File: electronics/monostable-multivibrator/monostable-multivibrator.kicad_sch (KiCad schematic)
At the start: 1 part, among them U1 NE555P

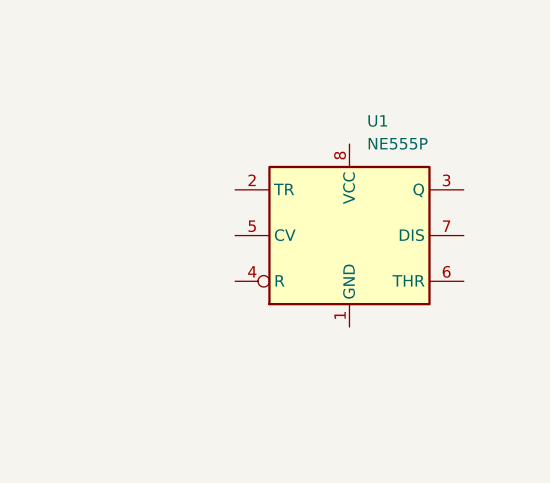
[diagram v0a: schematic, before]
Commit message: adding basic schematic
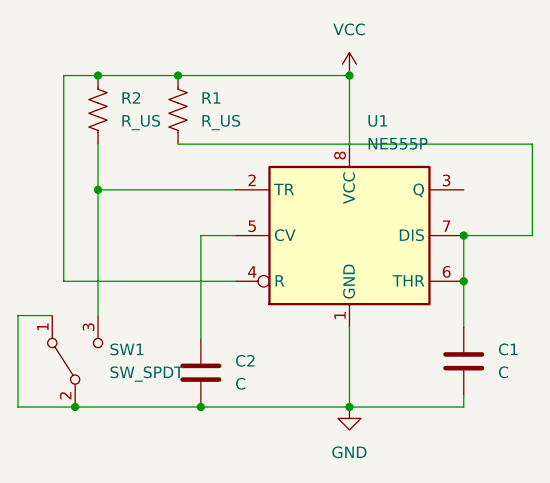
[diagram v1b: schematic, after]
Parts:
- added C1, C2: C, symbol Device:C
- added R1, R2: R_US, symbol Device:R_US
- added SW1: SW_SPDT, symbol Switch:SW_SPDT
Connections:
- net GND: now reaches U1.1 (GND)
- net GND: now also C1.2, C2.2, SW1.1 (A), SW1.2 (B)
- net at U1.2 (TR): now also R2.2, SW1.3 (C)
- net VCC: now reaches U1.4 (R)
- net VCC: now also U1.8 (VCC), R1.1, R2.1
- net at U1.5 (CV): now also C2.1
- net at U1.6 (THR): now also U1.7 (DIS), C1.1, R1.2

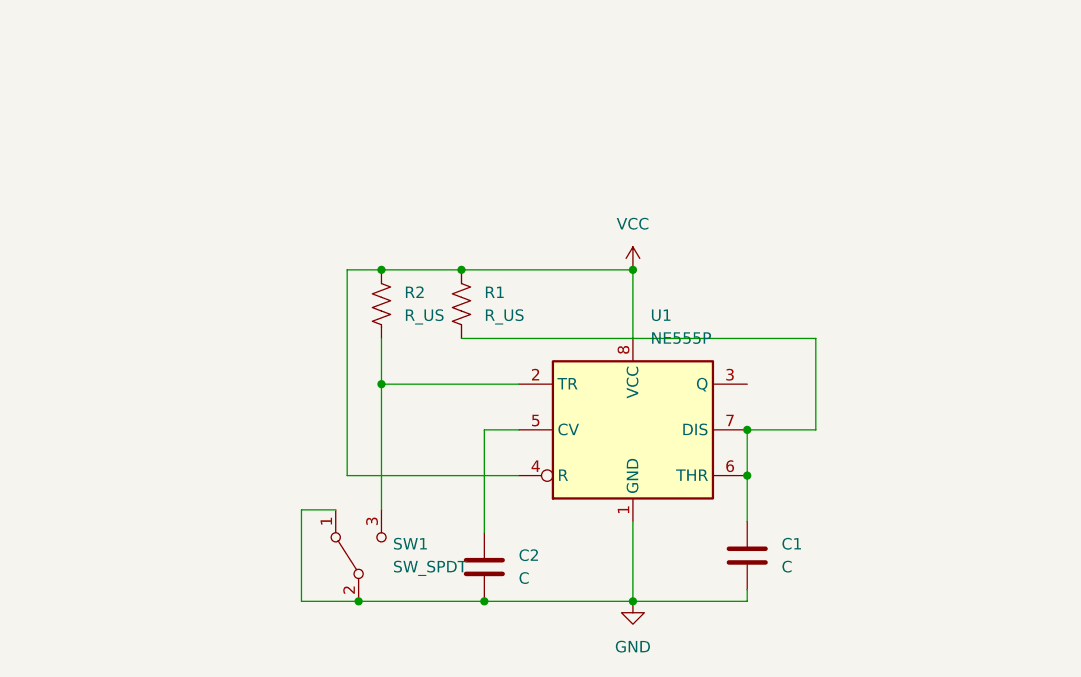
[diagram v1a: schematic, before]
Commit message: adding more components
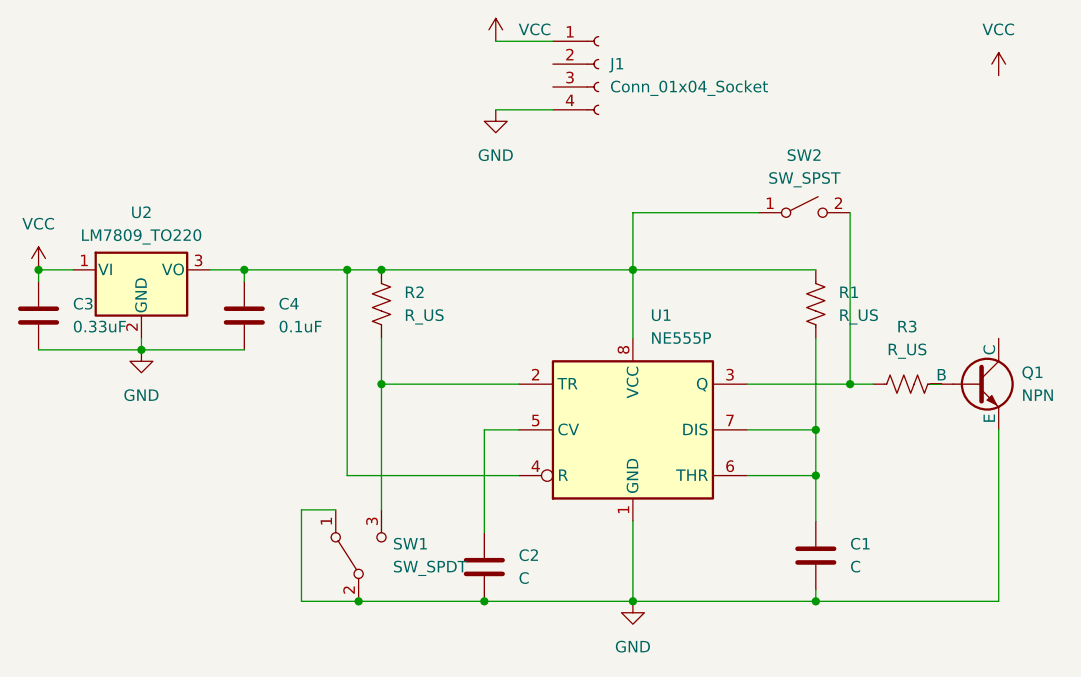
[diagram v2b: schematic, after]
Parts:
- added C3: 0.33uF, symbol Device:C
- added C4: 0.1uF, symbol Device:C
- added J1: Conn_01x04_Socket, symbol Connector:Conn_01x04_Socket
- added Q1: NPN, symbol Simulation_SPICE:NPN
- added R3: R_US, symbol Device:R_US
- added SW2: SW_SPST, symbol Switch:SW_SPST
- added U2: LM7809_TO220, Package_TO_SOT_THT:TO-220-3_Vertical, symbol Regulator_Linear:LM7809_TO220
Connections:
- net GND: now also C3.2, C4.2, J1.4 (Pin_4), Q1.3 (E), U2.2 (GND)
- net VCC: now also C3.1, J1.1 (Pin_1), U2.1 (VI); no longer R1.1, R2.1, U1.4 (R), U1.8 (VCC)
- net at U1.3 (Q): now also R3.1, SW2.2 (B)
- new net: Q1.2 (B), R3.2
- new net: C4.1, R1.1, R2.1, SW2.1 (A), U1.4 (R), U1.8 (VCC), U2.3 (VO)
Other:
- moved on the sheet: C1, R1

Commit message: more updates
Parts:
- removed J1: Conn_01x04_Socket, symbol Connector:Conn_01x04_Socket
- removed R2: R_US, symbol Device:R_US
- removed SW2: SW_SPST, symbol Switch:SW_SPST
- added J1, J2, J3, J4, J5, J6, J7, J8: Conn_01x01_Socket, symbol Connector:Conn_01x01_Socket
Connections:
- net GND: now also J2.1 (Pin_1)
- net VCC: now also J1.1 (Pin_1), J7.1 (Pin_1)
- net at R3.1, U1.3 (Q): now also J6.1 (Pin_1)
- net at Q1.1 (C): now also J8.1 (Pin_1)
- net at C4.1, R1.1, U1.4 (R)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: now also J3.1 (Pin_1), J5.1 (Pin_1)
- net at SW1.3 (C), U1.2 (TR): now also R1.2
- net at C1.1, U1.6 (THR), U1.7 (DIS): now also J4.1 (Pin_1); no longer R1.2
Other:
- moved on the sheet: R1

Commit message: mostly finished
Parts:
- removed J5, J6, J7, J8: Conn_01x01_Socket, symbol Connector:Conn_01x01_Socket
- removed U2: LM7809_TO220, Package_TO_SOT_THT:TO-220-3_Vertical, symbol Regulator_Linear:LM7809_TO220
- added D1, D2: 1N4001, Diode_THT:D_DO-41_SOD81_P10.16mm_Horizontal, symbol Diode:1N4001
- added JP1: Jumper_2_Open, symbol Jumper:Jumper_2_Open
- added R2: POT, symbol Device:R_US
- added SW2: SW_BYPASS, symbol Switch:SW_SPST
- added U2: LM7805_TO220, Package_TO_SOT_THT:TO-220-3_Vertical, symbol Regulator_Linear:LM7805_TO220
- C2: value C -> 10nF
- J1: value Conn_01x01_Socket -> VCC_IN
- J2: value Conn_01x01_Socket -> EXT_GND
- J3: value Conn_01x01_Socket -> LOAD_VIN
- J4: value Conn_01x01_Socket -> LOAD_COM
- Q1: value NPN -> 2N2222
- R1: value R_US -> 100K
- R3: value R_US -> 120
- SW1: value SW_SPDT -> SW_TRIG
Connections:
- net GND: now also C2.1, SW1.3 (C), D1.2 (A), U2.2 (GND); no longer C2.2, SW1.1 (A), SW1.2 (B)
- net VCC: now also J3.1 (Pin_1), JP1.1 (A), U2.1 (VI)
- net at R3.1: now also D2.1 (K), SW2.1 (A); no longer U1.3 (Q)
- net at C1.1, U1.6 (THR), U1.7 (DIS): now also R2.2; no longer J4.1 (Pin_1)
- net at Q1.1 (C): now also J4.1 (Pin_1), D1.1 (K)
- net at U1.5 (CV): now also C2.2; no longer C2.1
- net 555_VIN: now reaches C4.1, R1.1, U1.4 (R), U1.8 (VCC)
- net 555_VIN: now also JP1.2 (B), R2.1, SW2.2 (B), U2.3 (VO); no longer J3.1 (Pin_1)
- new net: SW1.2 (B), U1.2 (TR)
- new net: R1.2, SW1.1 (A)
- new net 555_OUT: D2.2 (A), U1.3 (Q)
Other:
- note added: "JUMPER IF VCC < 16V REG NOT NEEDED"
- note added: "T = 1.1 * R2 * C1"
- moved on the sheet: C1, C2, C3, C4, J1, J2, Q1, R1, R3, SW1, U1

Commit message: footprints
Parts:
- C1: footprint (none) -> Capacitor_THT:CP_Radial_D8.0mm_P3.80mm
- C2, C3, C4: footprint (none) -> Capacitor_THT:C_Disc_D3.0mm_W1.6mm_P2.50mm
- J1, J3, J4: footprint (none) -> Connector_PinHeader_1.00mm:PinHeader_1x01_P1.00mm_Horizontal
- J2: value EXT_GND -> GND_IN; footprint (none) -> Connector_PinHeader_1.00mm:PinHeader_1x01_P1.00mm_Horizontal
- JP1, R1, R2, R3: footprint (none) -> Resistor_THT:R_Axial_DIN0207_L6.3mm_D2.5mm_P2.54mm_Vertical
- Q1: footprint (none) -> Package_TO_SOT_THT:TO-92
- SW1: footprint (none) -> Connector_PinHeader_1.00mm:PinHeader_1x03_P1.00mm_Horizontal
- SW2: footprint (none) -> Connector_PinHeader_1.00mm:PinHeader_1x02_P1.00mm_Horizontal
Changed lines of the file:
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@@
       (effects (font (size 1.27 1.27)))
     )
-    (property "Footprint" "" (at 198.374 128.524 90)
+    (property "Footprint" "Resistor_THT:R_Axial_DIN0207_L6.3mm_D2.5mm_P2.54mm_Vertical" (at 198.374 128.524 90)
       (effects (font (size 1.27 1.27)) hide)
     )
@@
       (effects (font (size 1.27 1.27)) (justify left))
     )
-    (property "Footprint" "" (at 270.51 129.54 0)
+    (property "Footprint" "Package_TO_SOT_THT:TO-92" (at 270.51 129.54 0)
       (effects (font (size 1.27 1.27)) hide)
     )
@@
       (effects (font (size 1.27 1.27)))
     )
-    (property "Footprint" "" (at 74.93 122.2248 0)
+    (property "Footprint" "Capacitor_THT:C_Disc_D3.0mm_W1.6mm_P2.50mm" (at 74.93 122.2248 0)
       (effects (font (size 1.27 1.27)) hide)
     )
@@
       (effects (font (size 1.27 1.27)) (justify left))
     )
-    (property "Footprint" "" (at 214.63 97.79 0)
+    (property "Footprint" "Connector_PinHeader_1.00mm:PinHeader_1x01_P1.00mm_Horizontal" (at 214.63 97.79 0)
       (effects (font (size 1.27 1.27)) hide)
     )
@@
       (effects (font (size 1.27 1.27)) (justify right))
     )
-    (property "Footprint" "" (at 193.04 105.41 0)
+    (property "Footprint" "Connector_PinHeader_1.00mm:PinHeader_1x02_P1.00mm_Horizontal" (at 193.04 105.41 0)
       (effects (font (size 1.27 1.27)) hide)
     )
@@
       (effects (font (size 1.27 1.27)) (justify left))
     )
-    (property "Footprint" "" (at 214.63 102.87 0)
+    (property "Footprint" "Connector_PinHeader_1.00mm:PinHeader_1x01_P1.00mm_Horizontal" (at 214.63 102.87 0)
       (effects (font (size 1.27 1.27)) hide)
     )
@@
       (effects (font (size 1.27 1.27)))
     )
-    (property "Footprint" "" (at 99.06 57.15 0)
+    (property "Footprint" "Resistor_THT:R_Axial_DIN0207_L6.3mm_D2.5mm_P2.54mm_Vertical" (at 99.06 57.15 0)
       (effects (font (size 1.27 1.27)) hide)
     )
@@
       (effects (font (size 1.27 1.27)) (justify left))
     )
-    (property "Footprint" "" (at 143.256 112.014 90)
+    (property "Footprint" "Resistor_THT:R_Axial_DIN0207_L6.3mm_D2.5mm_P2.54mm_Vertical" (at 143.256 112.014 90)
       (effects (font (size 1.27 1.27)) hide)
     )
@@
       (effects (font (size 1.27 1.27)) (justify left))
     )
-    (property "Footprint" "" (at 81.026 104.394 90)
+    (property "Footprint" "Resistor_THT:R_Axial_DIN0207_L6.3mm_D2.5mm_P2.54mm_Vertical" (at 81.026 104.394 90)
       (effects (font (size 1.27 1.27)) hide)
     )
@@
       (effects (font (size 1.27 1.27)) (justify left))
     )
-    (property "Footprint" "" (at 107.6452 76.2 0)
+    (property "Footprint" "Capacitor_THT:C_Disc_D3.0mm_W1.6mm_P2.50mm" (at 107.6452 76.2 0)
       (effects (font (size 1.27 1.27)) hide)
     )
@@
       (effects (font (size 1.27 1.27)) (justify left))
     )
-    (property "Footprint" "" (at 143.2052 137.16 0)
+    (property "Footprint" "Capacitor_THT:CP_Radial_D8.0mm_P3.80mm" (at 143.2052 137.16 0)
       (effects (font (size 1.27 1.27)) hide)
     )
@@
       (effects (font (size 1.27 1.27)) (justify left))
     )
-    (property "Footprint" "" (at 99.06 24.13 0)
+    (property "Footprint" "Connector_PinHeader_1.00mm:PinHeader_1x01_P1.00mm_Horizontal" (at 99.06 24.13 0)
       (effects (font (size 1.27 1.27)) hide)
     )
@@
       (effects (font (size 1.27 1.27)) (justify right))
     )
-    (property "Footprint" "" (at 82.55 113.03 0)
+    (property "Footprint" "Connector_PinHeader_1.00mm:PinHeader_1x03_P1.00mm_Horizontal" (at 82.55 113.03 0)
       (effects (font (size 1.27 1.27)) hide)
     )
@@
       (effects (font (size 1.27 1.27)) (justify left))
     )
-    (property "Footprint" "" (at 83.5152 76.2 0)
+    (property "Footprint" "Capacitor_THT:C_Disc_D3.0mm_W1.6mm_P2.50mm" (at 83.5152 76.2 0)
       (effects (font (size 1.27 1.27)) hide)
     )
@@
       (effects (font (size 1.27 1.27)) (justify left))
     )
-    (property "Value" "EXT_GND" (at 100.33 30.48 0)
-      (effects (font (size 1.27 1.27)) (justify left))
-    )
-    (property "Footprint" "" (at 99.06 29.21 0)
-      (effects (font (size 1.27 1.27)) hide)
-    )
+    (property "Value" "GND_IN" (at 100.33 30.48 0)
+      (effects (font (size 1.27 1.27)) (justify left))
+    )
+    (property "Footprint" "Connector_PinHeader_1.00mm:PinHeader_1x01_P1.00mm_Horizontal" (at 99.06 29.21 0)
+      (effects (font (size 1.27 1.27)) hide)
+    )

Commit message: adjustments
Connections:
- net GND: no longer D1.2 (A)
- net VCC: now also D1.1 (K)
- net at J4.1 (Pin_1), Q1.1 (C): now also D1.2 (A); no longer D1.1 (K)
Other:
- moved on the sheet: D1, J3, J4, Q1, R3, SW2

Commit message: looking finished
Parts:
- removed Q1: 2N2222, Package_TO_SOT_THT:TO-92, symbol Simulation_SPICE:NPN
- added H2, H3: MountingHole_Pad, MountingHole:MountingHole_3.2mm_M3_DIN965_Pad_TopBottom, symbol Mechanical:MountingHole_Pad
- added Q1: 2N3904, Package_TO_SOT_THT:TO-92, symbol Transistor_BJT:2N3904
- J1, J2, J3, J4: footprint Connector_PinHeader_1.00mm:PinHeader_1x01_P1.00mm_Horizontal -> Connector_PinHeader_2.00mm:PinHeader_1x01_P2.00mm_Vertical
- R1, R2, R3: footprint Resistor_THT:R_Axial_DIN0207_L6.3mm_D2.5mm_P2.54mm_Vertical -> Resistor_THT:R_Axial_DIN0207_L6.3mm_D2.5mm_P7.62mm_Horizontal
- SW1: footprint Connector_PinHeader_1.00mm:PinHeader_1x03_P1.00mm_Horizontal -> Connector_PinHeader_2.00mm:PinHeader_1x03_P2.00mm_Vertical
- SW2: footprint Connector_PinHeader_1.00mm:PinHeader_1x02_P1.00mm_Horizontal -> Connector_PinHeader_2.00mm:PinHeader_1x02_P2.00mm_Vertical
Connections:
- net GND: now also H2.1, H3.1, Q1.1 (E)
- net at D1.2 (A), J4.1 (Pin_1): now also Q1.3 (C)
- net at R3.2: now also Q1.2 (B)
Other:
- moved on the sheet: R3

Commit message: adding important note
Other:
- note added: "CHANGE R3 IF 555_VIN > 5V"
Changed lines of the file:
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@@
     (stroke (width 0) (type default))
+  )
+  (text "CHANGE R3 IF 555_VIN > 5V" (at 189.23 153.67 0)
+    (effects (font (size 1.27 1.27)) (justify left bottom))
   )
   (text "JUMPER IF VCC < 16V\nREG NOT NEEDED" (at 87.63 48.26 0)
